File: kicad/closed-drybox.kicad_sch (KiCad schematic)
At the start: 0 parts

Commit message: init KiCad
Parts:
- added J1: Power_Jack, Connector_BarrelJack:BarrelJack_Horizontal, symbol CustomSymbols:Power_Jack
- added M1, M2: Fan, Connector_JST:JST_XH_S2B-XH-A_1x02_P2.50mm_Horizontal, symbol Motor:Fan
- added Q1, Q2, Q3, Q? (x4): AO3400A, Package_TO_SOT_SMD:SOT-23_Handsoldering, symbol Transistor_FET:AO3400A
- added R1, R? (x4): Heater, Connector_JST:JST_XH_S2B-XH-A_1x02_P2.50mm_Horizontal, symbol Device:Heater
- added SW1: SW_PWR, Connector_PinHeader_2.54mm:PinHeader_1x02_P2.54mm_Vertical, symbol CustomSymbols:SW_PWR
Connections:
- new net: Q?.3 (D), R?.2 (x4)
- new net: M1.2 (-), Q2.3 (D)
- new net: M2.2 (-), Q3.3 (D)
- new net: J1.1, SW1.1
- new net: Q1.3 (D), R1.2
- new net +12V: M1.1 (+), M2.1 (+), R1.1, R?.1, R?.1, R?.1, R?.1, SW1.2
- new net FAN1: Q2.1 (G)
- new net FAN2: Q3.1 (G)
- new net GND: J1.2, J1.3 (MP), Q1.2 (S), Q2.2 (S), Q3.2 (S), Q?.2 (S), Q?.2 (S), Q?.2 (S), Q?.2 (S)
- new net HEAT1: Q1.1 (G)
- new net HEAT2: Q?.1 (G)
- new net HEAT3: Q?.1 (G)
- new net HEAT4: Q?.1 (G)
- new net HEAT5: Q?.1 (G)
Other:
- note added: "Heater"
- note added: "Power input"
- title: (none) -> closed-drybox

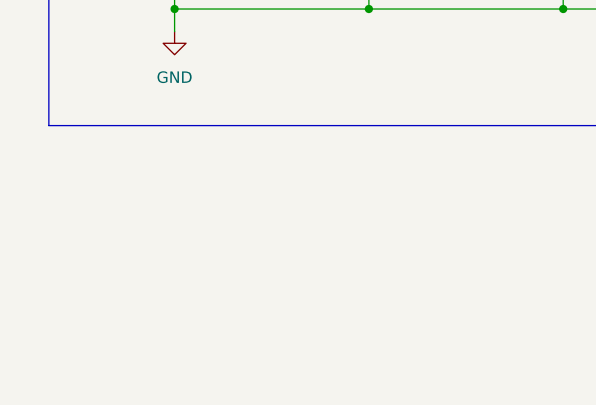
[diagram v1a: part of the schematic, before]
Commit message: add 1117 3.3V
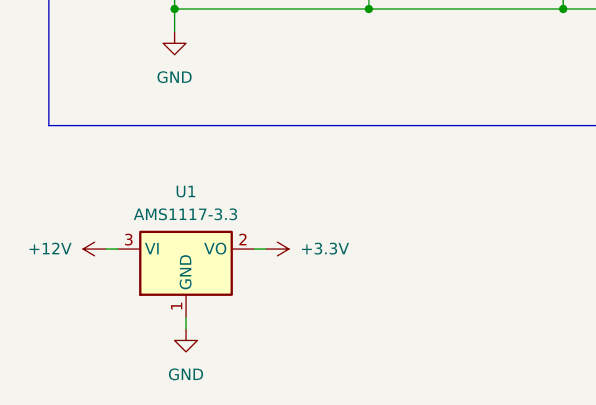
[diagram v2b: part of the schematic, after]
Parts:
- added U1: AMS1117-3.3, Package_TO_SOT_SMD:SOT-223-3_TabPin2, symbol Regulator_Linear:AMS1117-3.3
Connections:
- net +12V: now also U1.3 (VI)
- net GND: now also U1.1 (GND)
- new net +3.3V: U1.2 (VO)

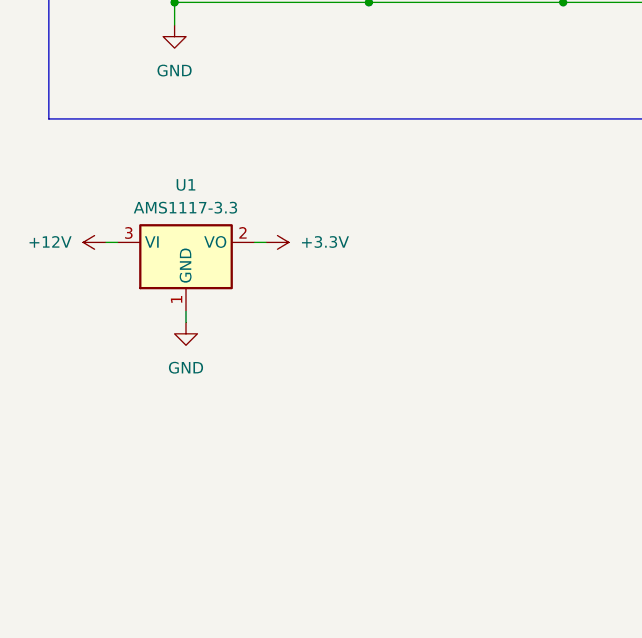
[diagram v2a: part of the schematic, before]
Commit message: add 1117 5V
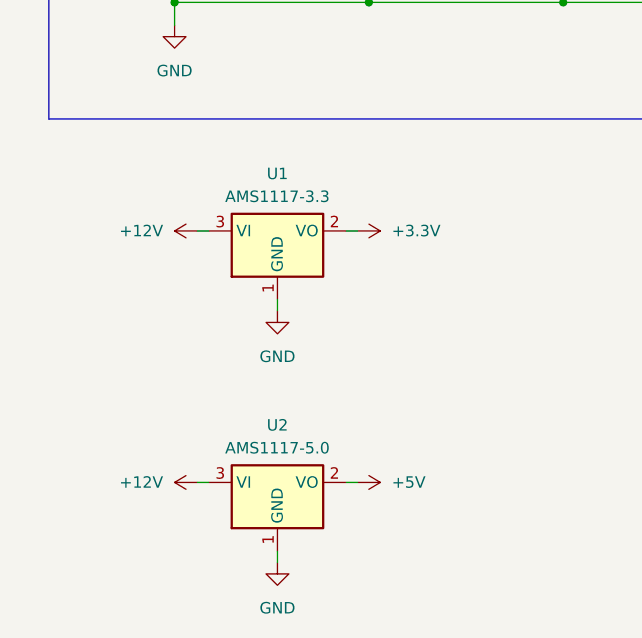
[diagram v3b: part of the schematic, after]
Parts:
- added U2: AMS1117-5.0, Package_TO_SOT_SMD:SOT-223-3_TabPin2, symbol Regulator_Linear:AMS1117-5.0
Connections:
- net +12V: now also U2.3 (VI)
- net GND: now also U2.1 (GND)
- new net +5V: U2.2 (VO)
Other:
- moved on the sheet: U1

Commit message: add #LCSC
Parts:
- M1, M2: LCSC (none) -> C158012
- Q1, Q2, Q3: LCSC (none) -> C20917
- Q4, Q5, Q6, Q7: renamed from Q?; LCSC (none) -> C20917
- U1: LCSC (none) -> C6186
- U2: LCSC (none) -> C6187
- gave numbers to parts that had none: 4
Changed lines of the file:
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@@
 		(dnp no)
 		(fields_autoplaced yes)
-		(property "Reference" "R?"
+		(property "Reference" "R3"
 			(at 74.93 68.5799 0)
 			(effects
@@
 			(project "closed-drybox"
 				(path "/99399f2a-756c-4718-9b6a-bb37855e6538"
-					(reference "R?")
+					(reference "R3")
 					(unit 1)
 				)
@@
 			)
 		)
+		(property "LCSC" "C20917"
+			(at 152.4 55.8799 0)
+			(effects
+				(font
+					(size 1.27 1.27)
+				)
+				(hide yes)
+			)
+		)
 		(pin "3"
 		)
@@
 			)
 		)
+		(property "LCSC" "C158012"
+			(at 153.67 36.8299 0)
+			(effects
+				(font
+					(size 1.27 1.27)
+				)
+				(hide yes)
+			)
+		)
 		(pin "2"
 		)
@@
 			)
 		)
+		(property "LCSC" "C20917"
+			(at 177.8 55.8799 0)
+			(effects
+				(font
+					(size 1.27 1.27)
+				)
+				(hide yes)
+			)
+		)
 		(pin "3"
 		)
@@
 			)
 		)
+		(property "LCSC" "C20917"
+			(at 33.02 80.0099 0)
+			(effects
+				(font
+					(size 1.27 1.27)
+				)
+				(hide yes)
+			)
+		)
 		(pin "3"
 		)
@@
 		(dnp no)
 		(fields_autoplaced yes)
-		(property "Reference" "R?"
+		(property "Reference" "R2"
 			(at 53.34 68.5799 0)
 			(effects
@@
 			(project "closed-drybox"
 				(path "/99399f2a-756c-4718-9b6a-bb37855e6538"
-					(reference "R?")
+					(reference "R2")
 					(unit 1)
 				)
@@
 		(dnp no)
 		(fields_autoplaced yes)
-		(property "Reference" "R?"
+		(property "Reference" "R5"
 			(at 118.11 68.5799 0)
 			(effects
@@
 			(project "closed-drybox"
 				(path "/99399f2a-756c-4718-9b6a-bb37855e6538"
-					(reference "R?")
+					(reference "R5")
 					(unit 1)
 				)
@@
 		(on_board yes)
 		(dnp no)
-		(property "Reference" "Q?"
+		(property "Reference" "Q7"
 			(at 119.38 80.0099 0)
 			(effects
@@
 			)
 		)
+		(property "LCSC" "C20917"
+			(at 119.38 80.0099 0)
+			(effects
+				(font
+					(size 1.27 1.27)
+				)
+				(hide yes)
+			)
+		)
 		(pin "3"
 		)
@@
 			(project "closed-drybox"
 				(path "/99399f2a-756c-4718-9b6a-bb37855e6538"
-					(reference "Q?")
+					(reference "Q7")
 					(unit 1)
 				)
@@
 		(on_board yes)
 		(dnp no)
-		(property "Reference" "Q?"
+		(property "Reference" "Q5"
 			(at 76.2 80.0099 0)
 			(effects
@@
 			)
 		)
+		(property "LCSC" "C20917"
+			(at 76.2 80.0099 0)
+			(effects
+				(font
+					(size 1.27 1.27)
+				)
+				(hide yes)
+			)
+		)
 		(pin "3"
 		)
@@
 			(project "closed-drybox"
 				(path "/99399f2a-756c-4718-9b6a-bb37855e6538"
-					(reference "Q?")
+					(reference "Q5")
 					(unit 1)
 				)
@@
 			)
 		)
+		(property "LCSC" "C6187"
+			(at 40.64 135.89 0)
+			(effects
+				(font
+					(size 1.27 1.27)
+				)
+				(hide yes)
+			)
+		)
 		(pin "2"
 		)
@@
 		(on_board yes)
 		(dnp no)
-		(property "Reference" "Q?"
+		(property "Reference" "Q6"
 			(at 97.79 80.0099 0)
 			(effects
@@
 			)
 		)
+		(property "LCSC" "C20917"
+			(at 97.79 80.0099 0)
+			(effects
+				(font
+					(size 1.27 1.27)
+				)
+				(hide yes)
+			)
+		)
 		(pin "3"
 		)
@@
 			(project "closed-drybox"
 				(path "/99399f2a-756c-4718-9b6a-bb37855e6538"
-					(reference "Q?")
+					(reference "Q6")
 					(unit 1)
 				)
@@
 		(on_board yes)
 		(dnp no)
-		(property "Reference" "Q?"
+		(property "Reference" "Q4"
 			(at 54.61 80.0099 0)
 			(effects
@@
 			)
 		)
+		(property "LCSC" "C20917"
+			(at 54.61 80.0099 0)
+			(effects
+				(font
+					(size 1.27 1.27)
+				)
+				(hide yes)
+			)
+		)
 		(pin "3"
 		)
@@
 			(project "closed-drybox"
 				(path "/99399f2a-756c-4718-9b6a-bb37855e6538"
-					(reference "Q?")
+					(reference "Q4")
 					(unit 1)
 				)
@@
 			)
 		)
+		(property "LCSC" "C6186"
+			(at 40.64 107.95 0)
+			(effects
+				(font
+					(size 1.27 1.27)
+				)
+				(hide yes)
+			)
+		)
 		(pin "1"
 		)
@@
 		(dnp no)
 		(fields_autoplaced yes)
-		(property "Reference" "R?"
+		(property "Reference" "R4"
 			(at 96.52 68.5799 0)
 			(effects
@@
 			(project "closed-drybox"
 				(path "/99399f2a-756c-4718-9b6a-bb37855e6538"
-					(reference "R?")
+					(reference "R4")
 					(unit 1)
 				)
@@
 			(effects
 				(font
+					(size 1.27 1.27)
+				)
+				(hide yes)
+			)
+		)
+		(property "LCSC" "C158012"
+			(at 179.07 36.8299 0)
+			(effects
+				(font

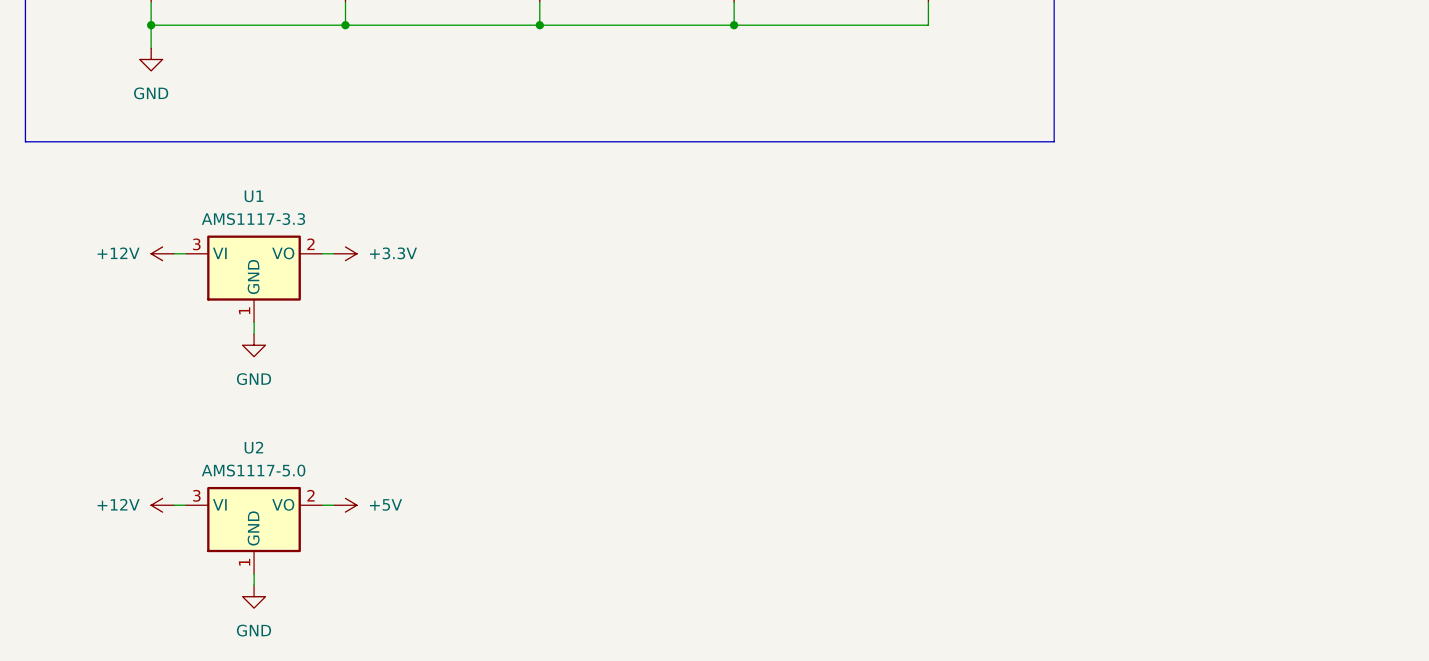
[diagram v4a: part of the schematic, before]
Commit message: add example
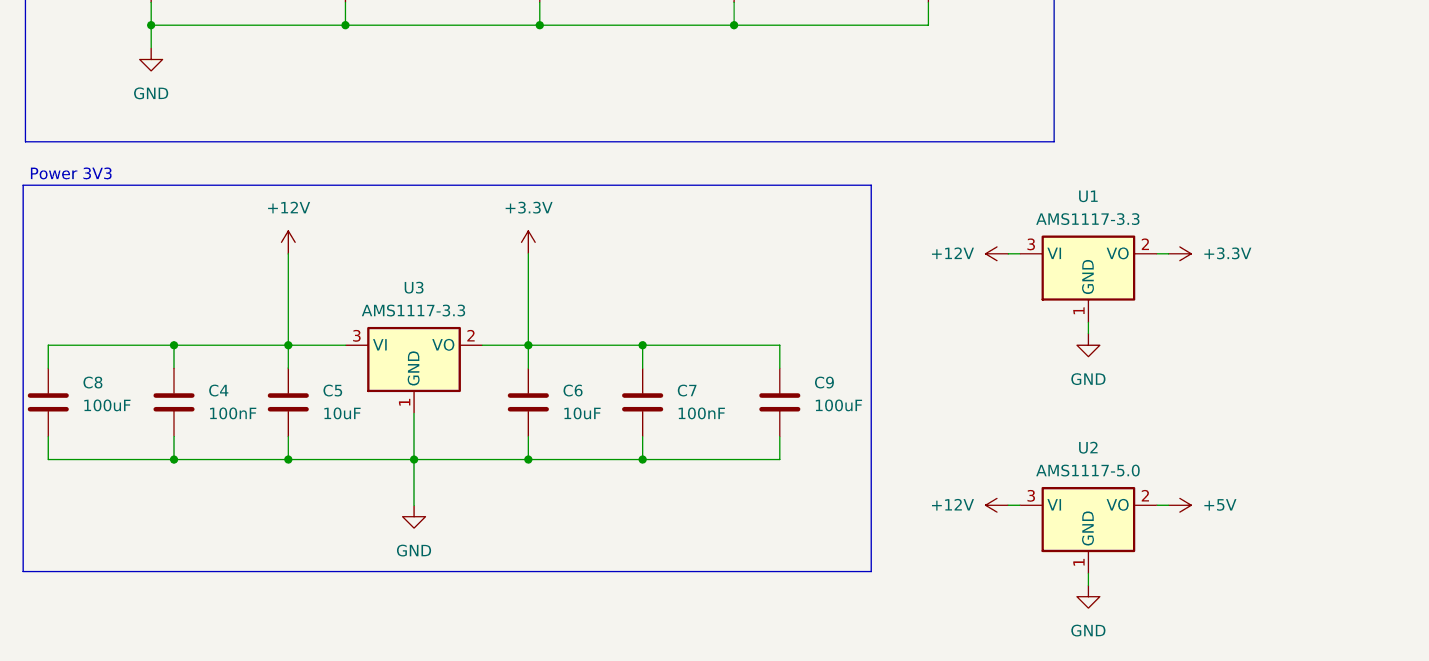
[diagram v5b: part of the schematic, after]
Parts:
- added C4, C7: 100nF, Capacitor_SMD:C_0603_1608Metric, symbol Device:C
- added C5, C6: 10uF, Capacitor_SMD:C_0603_1608Metric, symbol Device:C
- added C8, C9: 100uF, Capacitor_SMD:C_1206_3216Metric, symbol Device:C
- added U3: AMS1117-3.3, Package_TO_SOT_SMD:SOT-223-3_TabPin2, symbol Regulator_Linear:AMS1117-3.3
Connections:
- net +12V: now also C4.1, C5.1, C8.1, U3.3 (VI)
- net +3.3V: now also C6.1, C7.1, C9.1, U3.2 (VO)
- net GND: now also C4.2, C5.2, C6.2, C7.2, C8.2, C9.2, U3.1 (GND)
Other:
- note added: "Power 3V3"
- moved on the sheet: U1, U2

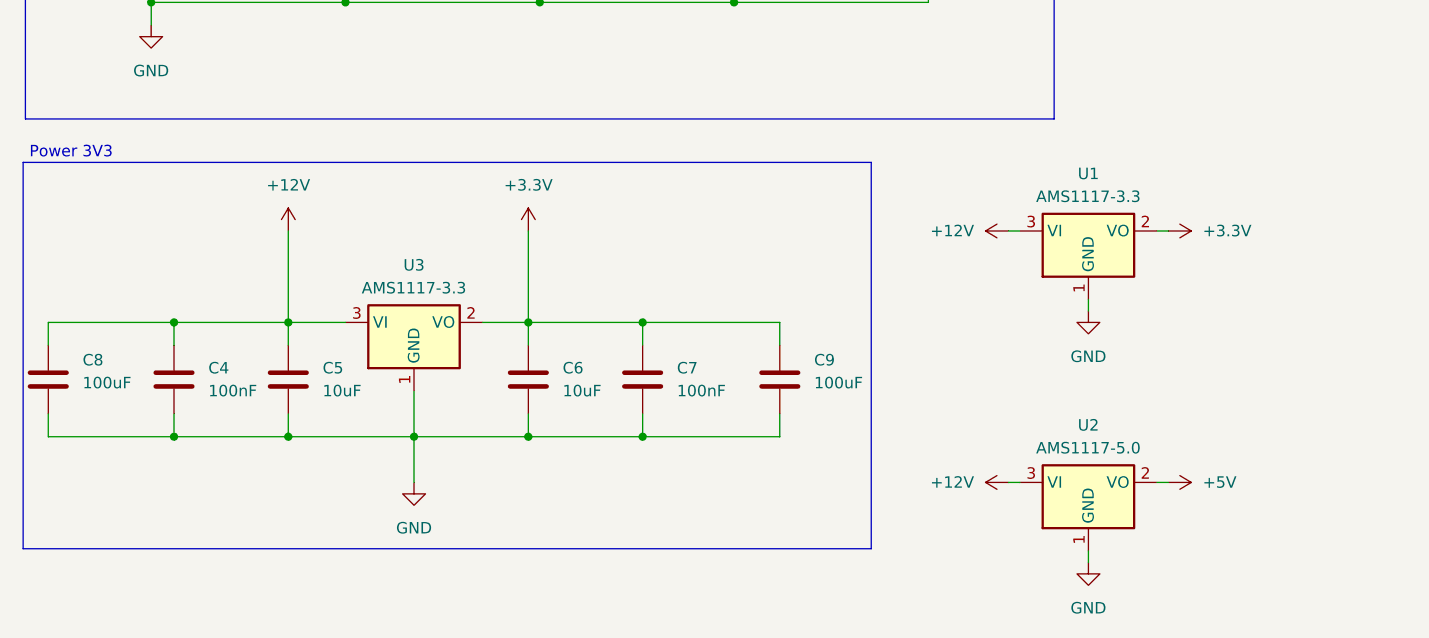
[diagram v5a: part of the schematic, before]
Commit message: correct Capacitators
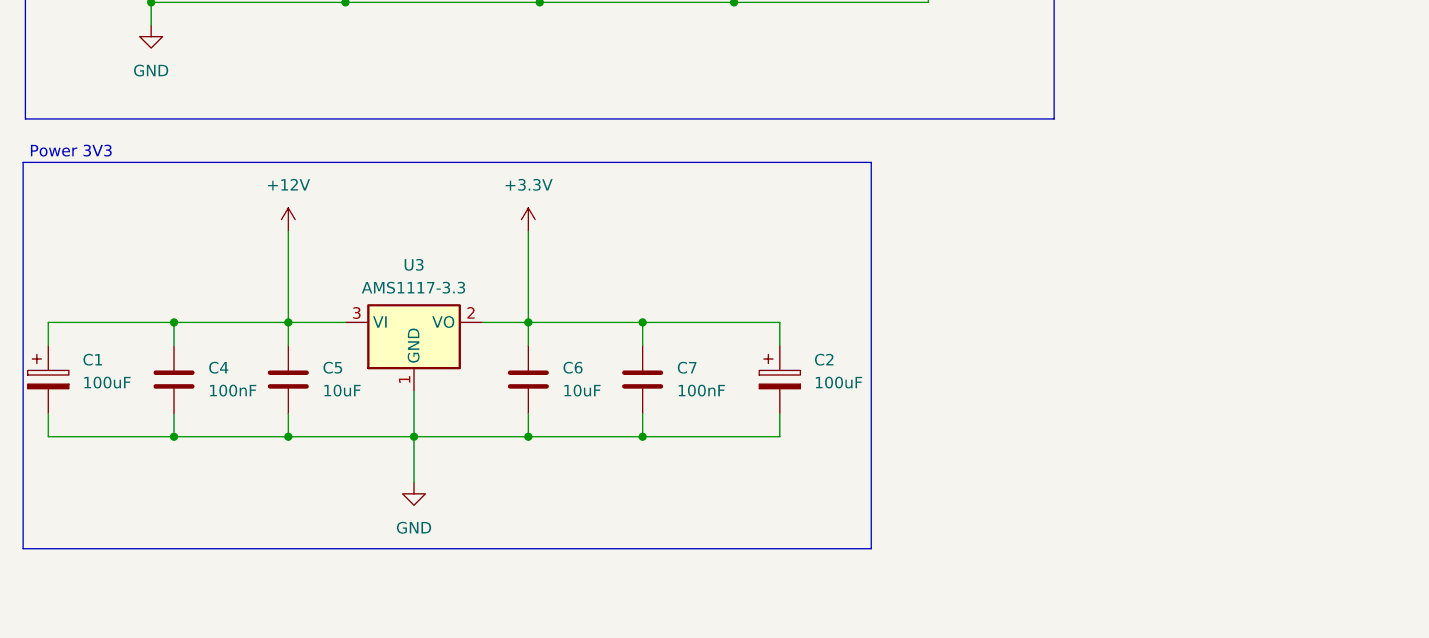
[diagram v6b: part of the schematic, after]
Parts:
- removed C8, C9: 100uF, Capacitor_SMD:C_1206_3216Metric, symbol Device:C
- removed U1: AMS1117-3.3, Package_TO_SOT_SMD:SOT-223-3_TabPin2, symbol Regulator_Linear:AMS1117-3.3
- removed U2: AMS1117-5.0, Package_TO_SOT_SMD:SOT-223-3_TabPin2, symbol Regulator_Linear:AMS1117-5.0
- added C1, C2: 100uF, symbol Device:C_Polarized
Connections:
- net +12V: now also C1.1
- net +3.3V: now also C2.1
- net GND: now also C1.2, C2.2
